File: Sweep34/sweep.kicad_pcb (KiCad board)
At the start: 2 copper layers, 110 x 88.3 mm, 21 parts, among them J1 MJ-4PP-9, SW10 SW_PUSH, SW11 SW_PUSH, SW12 SW_PUSH, SW14 SW_PUSH, SW15 SW_PUSH, SW16 SW_PUSH, SW17 SW_PUSH, SW18 SW_PUSH, SW2 SW_PUSH, SW20 SW_PUSH, SW21 SW_PUSH, SW3 SW_PUSH, SW4 SW_PUSH, SW5 SW_PUSH, SW6 SW_PUSH, SW8 SW_PUSH, SW9 SW_PUSH, U1 ProMicro

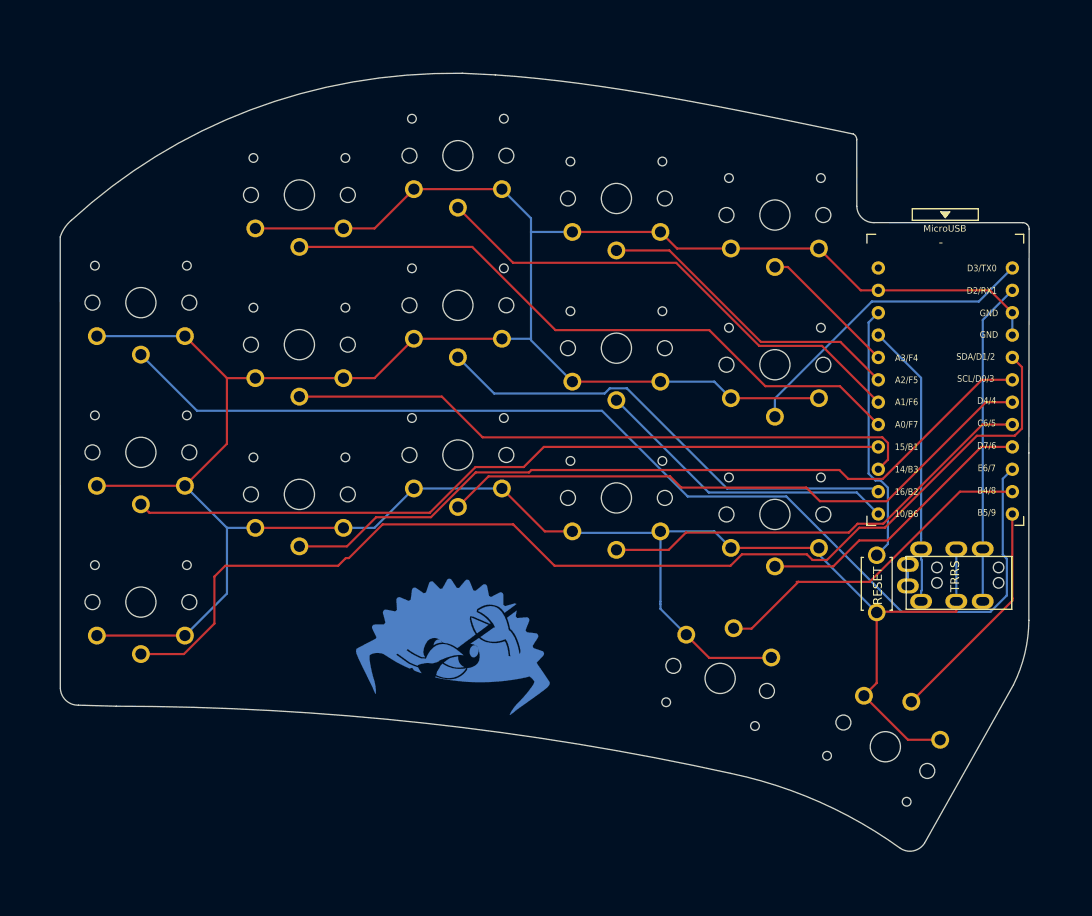
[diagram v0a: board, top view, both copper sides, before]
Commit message: superflous routing.
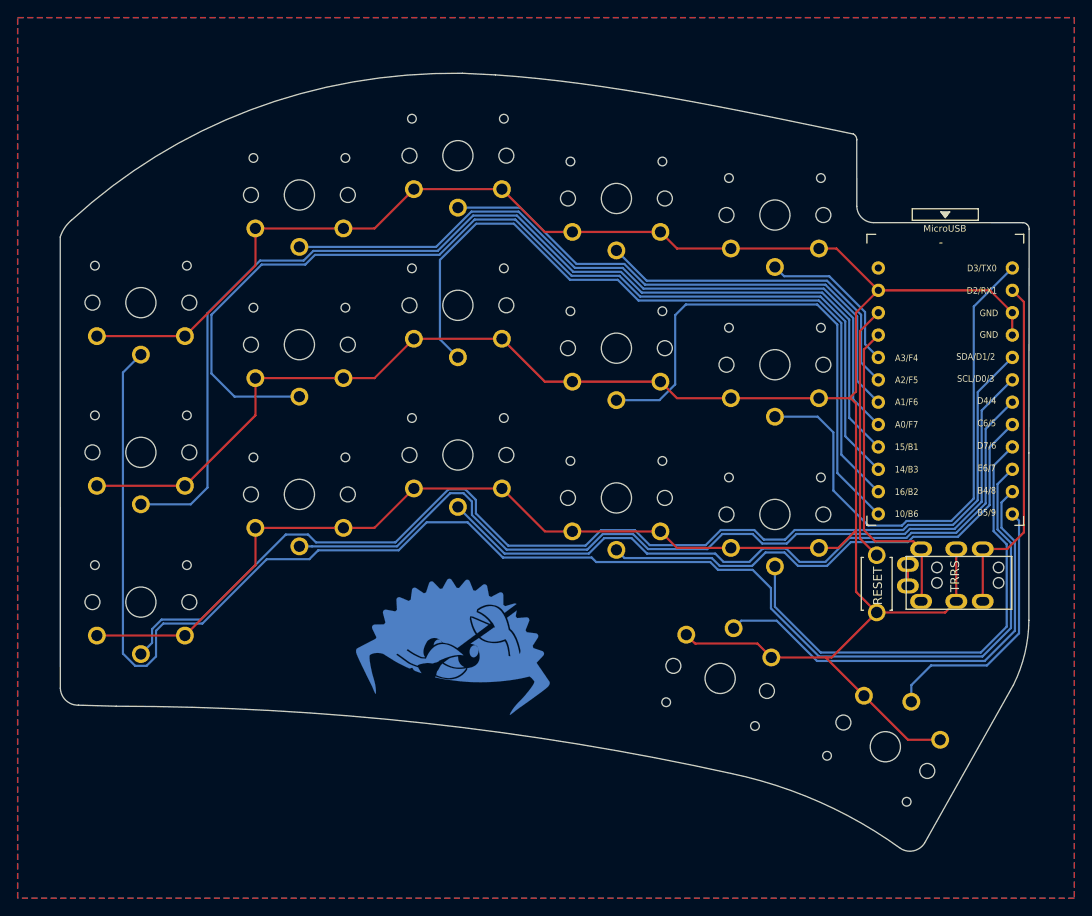
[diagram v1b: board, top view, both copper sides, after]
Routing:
- net row3: track 126.2 -> 173.0 mm
- net col5: track 72.5 -> 117.3 mm
- net col4: track 87.2 -> 126.3 mm
- net Net-(U1-Pad14): track 54.6 -> 84.7 mm
- net LED: track 35.2 -> 60.8 mm
- net row2: track 32.6 -> 56.2 mm
- net Net-(U1-Pad13): track 35.1 -> 58.6 mm
- net GND: track 395.8 -> 415.1 mm
- net Net-(U1-Pad11): track 38.3 -> 52.6 mm
- net SCL: track 89.6 -> 103.4 mm
- net row0: track 70.2 -> 80.7 mm
- net col3: track 74.1 -> 82.8 mm
- net row1: track 50.9 -> 57.5 mm
- net col2: track 56.9 -> 61.2 mm
- net Net-(U1-Pad12): track 26.2 -> 30.4 mm
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- added copper zone on B.Cu, net (none)
- added copper zone on F.Cu, net (none)
